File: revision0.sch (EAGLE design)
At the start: 105 parts, among them IC1 MSP430FR698X(1)80-PIN_PN, IC3 FT232RL

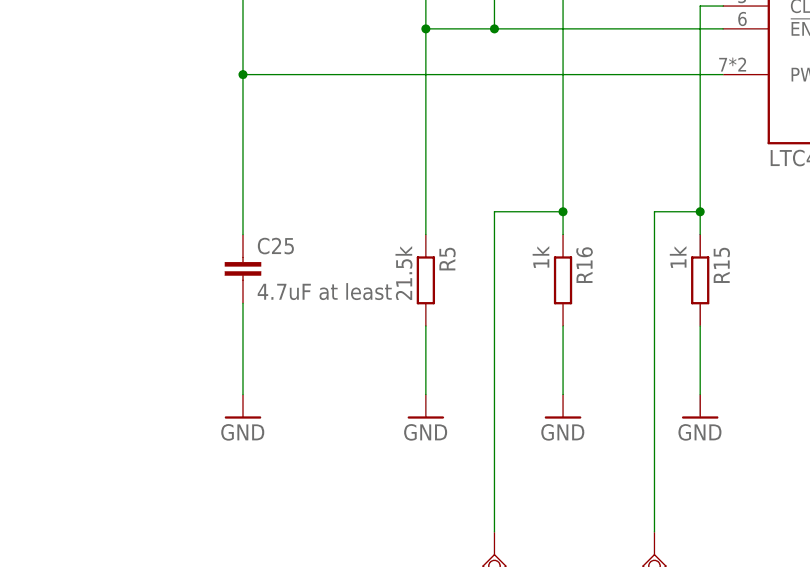
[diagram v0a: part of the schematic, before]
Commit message: fix power-switcher voltage divider resistor value
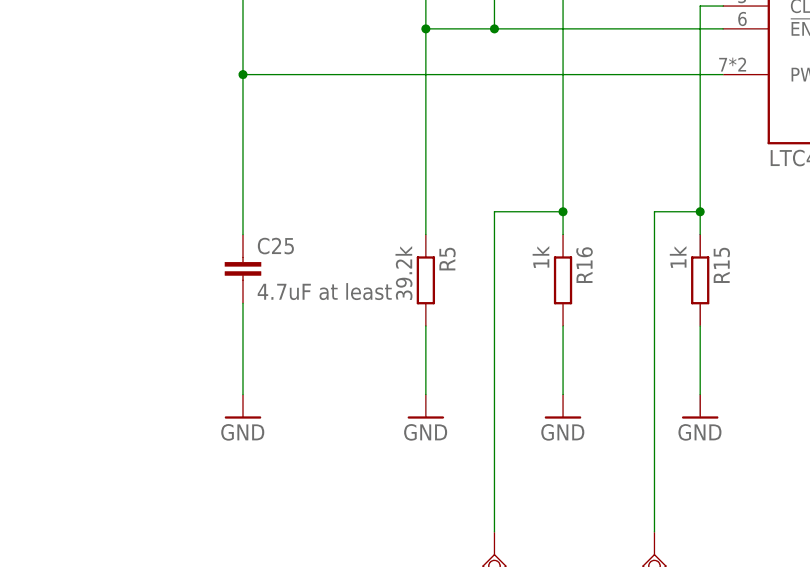
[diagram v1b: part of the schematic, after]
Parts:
- R5: value 21.5k -> 39.2k
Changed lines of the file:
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@@
 <part name="U$2" library="tagps" deviceset="LTC4415" device=""/>
 <part name="R4" library="tagps" deviceset="R-EU_" device="R0805" value="100k"/>
-<part name="R5" library="tagps" deviceset="R-EU_" device="R0805" value="21.5k"/>
+<part name="R5" library="tagps" deviceset="R-EU_" device="R0805" value="39.2k"/>
 <part name="GND15" library="supply1" deviceset="GND" device=""/>
 <part name="P+2" library="tagps" deviceset="VCC" device="" value="VCC_BATT_IN"/>

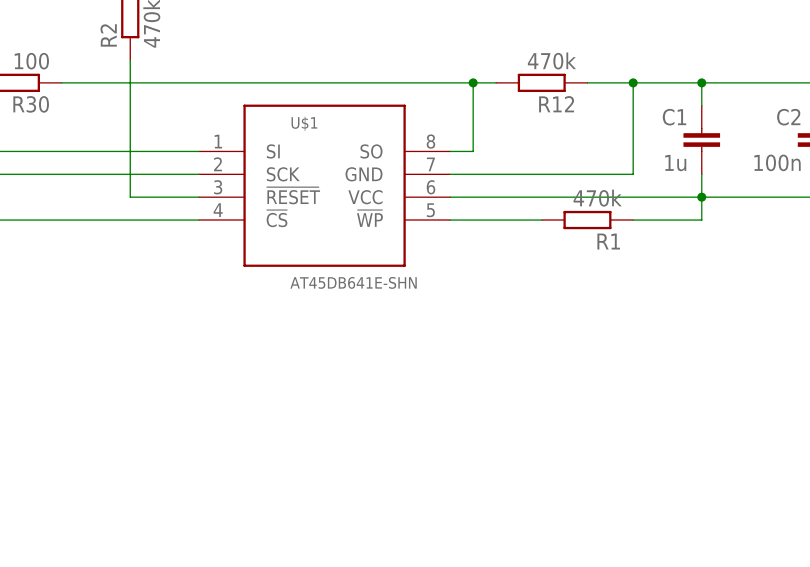
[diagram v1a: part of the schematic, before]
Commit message: Fix SPI flash package foot print on PCB
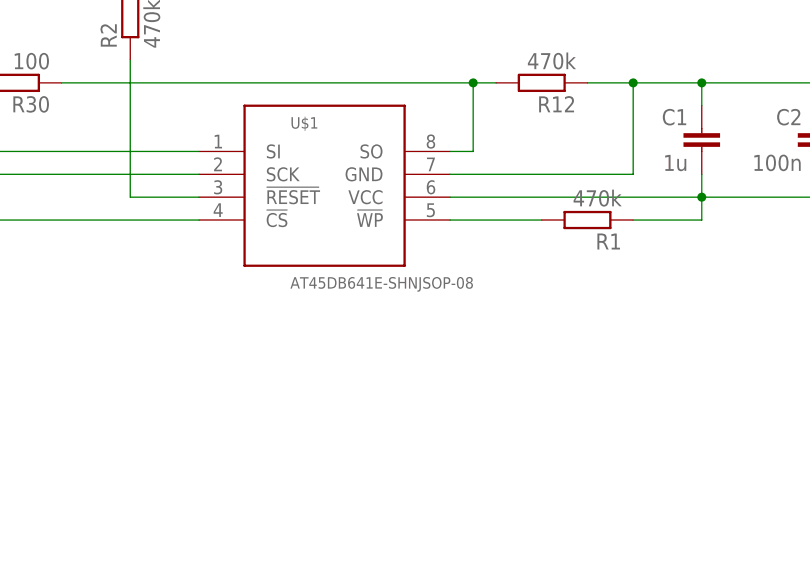
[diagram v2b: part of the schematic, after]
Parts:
- U$1: value AT45DB641E-SHN -> AT45DB641E-SHNJSOP-08; device tagps:AT45DB641E-SHN -> tagps:AT45DB641E-SHNJSOP-08
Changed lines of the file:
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@@
 <part name="R14" library="tagps" deviceset="R-EU_" device="R0805" value="220"/>
 <part name="GND28" library="supply1" deviceset="GND" device=""/>
-<part name="U$1" library="tagps" deviceset="AT45DB641E-SHN" device=""/>
+<part name="U$1" library="tagps" deviceset="AT45DB641E-SHN" device="JSOP-08"/>
 <part name="P+18" library="tagps" deviceset="VCC" device="" value="VCC"/>
 <part name="R1" library="tagps" deviceset="R-EU_" device="R0805" value="470k"/>

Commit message: Resize Cc and Rs from 0805->0603
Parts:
- C1, C10, C11, C12, C13, C14, C15, C16, C17, C19, C2, C20, C21, C23, C26, C29, C3, C4, C5, C6, C7, C8, C9: device tagps:C-EUC0805 -> tagps:C-EUC0603
- R1, R10, R11, R12, R13, R14, R15, R16, R17, R2, R22, R23, R24, R25, R26, R27, R28, R29, R3, R30, R31, R32, R33, R34, R35, R4, R5, R6, R7, R8, R9: device tagps:R-EU_R0805 -> tagps:R-EU_R0603

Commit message: Split board to 2 pieces, remove ADC battery input (was senseless)
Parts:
- removed C16, C23: 100n, tagps:C-EUC0603
- removed C17, C29: 1u, tagps:C-EUC0603
- removed FB1, FB2, FB3: 0, tagps:R-EU_R0805
- removed R28: 0, tagps:R-EU_R0603
- removed SV1: (no value), tagps:FE07W
- removed TP-GPSPWR, TP-GPSPWR1, TP-GPSRX, TP-GPSRX1, TP-GPSTX, TP-GPSTX1: TPSQTP10R, tagps:TPSQTP10R
- removed TP1: TPSQTP16R, tagps:TPSQTP16R
- removed U$3, U$7: MAX-8C-0, tagps:MAX-8C-0
- added R18: 0, tagps:R-EU_R0603
- added R19, R20: 100, tagps:R-EU_R0603
- added R21: 33k, tagps:R-EU_R0603
- G2: value BATTERY -> BATTERYTAP5-45; device tagps:BATTERY -> tagps:BATTERYTAP5-45
- JP1: device tagps:PINHD-1X7/90 -> tagps:PINHD-1X4
- JP2: device tagps:JP1Q -> tagps:PINHD-1X4
- R24: value 100k -> 33k
- R25: value 100k -> 0
- TP-PWRBATT, TP-PWRUSB: value TPSQPAD1-13 -> TPSQTP10R; device tagps:TPSQPAD1-13 -> tagps:TPSQTP10R
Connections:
- removed net ANTENNA: TP1.TP, U$3.RF_IN
- removed net GPS-RX: FB1.2, JP1.2, R24.1, TP-GPSRX.TP
- removed net GPS-TIMEPULSE: JP1.5, R28.1
- removed net GPS-TX: FB2.2, JP1.3, R25.1, TP-GPSTX.TP
- removed net GPS-WAKEUP: JP1.4, R26.1
- removed net N$21: FB3.1, U$3.TIMEPULSE
- removed net N$50: FB6.1, U$6.TIMEPULSE, U$7.TIMEPULSE
- removed net N$51: FB2.1, U$3.TXD
- removed net N$52: FB1.1, U$3.RXD
- removed net N$9: FB3.2, R28.2
- removed net PWR_GPS_SENSE: C16.2, C17.1, JP1.7, R24.2, R25.2, TP-GPSPWR.TP, U$3.VCC, U$3.VCC_IO, U$3.V_BCKP
- new net FT232-RX: JP1.3, R10.2, R20.2, TP-USBRX.TP
- new net FT232-TX: JP1.2, R8.2, R9.2, TP-USBTX.TP
- new net N$29: IC3.USBDP, R26.2
- new net N$4: IC3.RXD, R20.1
- new net N$60: FB6.1, U$6.TIMEPULSE
- new net VCCUSBGPS: C24.2, JP2.1, R4.1, R7.2, U$2.PWRI1
- net ADC-BATT: no longer IC1.P9.7/ESICI3/A15/C15
- net GND: now also JP1.4, JP2.4; no longer C16.1, C17.2, C23.1, C29.2, JP1.1, JP1.6, SV1.2, SV1.7, U$3.GND, U$7.GND
- net MB-GPS-RX: no longer SV1.6, TP-GPSRX1.TP
- net MB-GPS-TIMEPULSE: no longer SV1.3
- net MB-GPS-TX: no longer SV1.5, TP-GPSTX1.TP
- net MB-GPS-WAKEUP: no longer SV1.4
- net MB-PWR_GPS_SENSE: no longer C23.2, C29.1, SV1.1, TP-GPSPWR1.TP, U$7.VCC, U$7.VCC_IO, U$7.V_BCKP
- net MCU-RX-FT232: now also R19.2, R21.2; no longer R8.2, R9.2, TP-USBTX.TP
- net MCU-TX-FT232: now also JP2.2; no longer IC3.RXD, R10.2, TP-USBRX.TP
- net N$12: now also R26.1; no longer IC3.USBDP
- net N$15: no longer U$7.RXD
- net N$2: now also R24.2
- net N$26: now also R18.1, R25.1; no longer JP2.1
- net N$46: no longer U$7.EXTINT
- net N$49: no longer U$7.TXD
- net N$8: now also JP2.3, R19.1; no longer R26.2, U$3.EXTINT
- net VCC: now also R18.2, R21.1, R24.1, R25.2; no longer JP2.2
- net VCCUSB: now also JP1.1; no longer C24.2, R4.1, R7.2, U$2.PWRI1
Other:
- moved on the sheet: R24, R25, R26, S2, TP-VCC

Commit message: Remove UART pullups and button to make it even smaller
Removed GPS and USB pullups (do not forget to add them
to the MCU IOs!), removed one button, removed unnecesary
GPS ferrite beads
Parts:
- removed FB4, FB5, FB6: 0, tagps:R-EU_R0805
- removed R17, R33: 100k, tagps:R-EU_R0603
- removed R21, R24: 33k, tagps:R-EU_R0603
- removed S3: (no value), tagps:SWITCH-10-XX
- added R28: 100, tagps:R-EU_R0603
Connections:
- removed net N$15: FB4.1, U$6.RXD
- removed net N$49: FB5.1, U$6.TXD
- removed net N$60: FB6.1, U$6.TIMEPULSE
- removed net SW-CHECK-BATT-MEM: IC1.P3.6/UCA1CLK/TB0.2/S19, S3.P, S3.P1
- new net N$45: IC1.P3.5/UCA1SOMI/UCA1RXD/TB0.1/S20, R28.1
- net MB-GPS-RX: now also U$6.RXD; no longer FB4.2, R17.1
- net MB-GPS-TX: now also R28.2, U$6.TXD; no longer FB5.2, IC1.P3.5/UCA1SOMI/UCA1RXD/TB0.1/S20, R33.1
- net MB-PWR_GPS_SENSE: no longer R17.2, R33.2
- net MCU-RX-FT232: no longer R21.2
- net N$2: no longer R24.2
- net N$47: now also U$6.TIMEPULSE; no longer FB6.2
- net VCC: no longer R21.1, R24.1, S3.S, S3.S1
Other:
- moved on the sheet: C13, C14, R34, R35, U$6
